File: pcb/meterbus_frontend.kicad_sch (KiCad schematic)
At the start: 34 parts, among them Q3 AO3400A, U1 78L05G, U3 ISO6721RBDR, U5 74HC14D

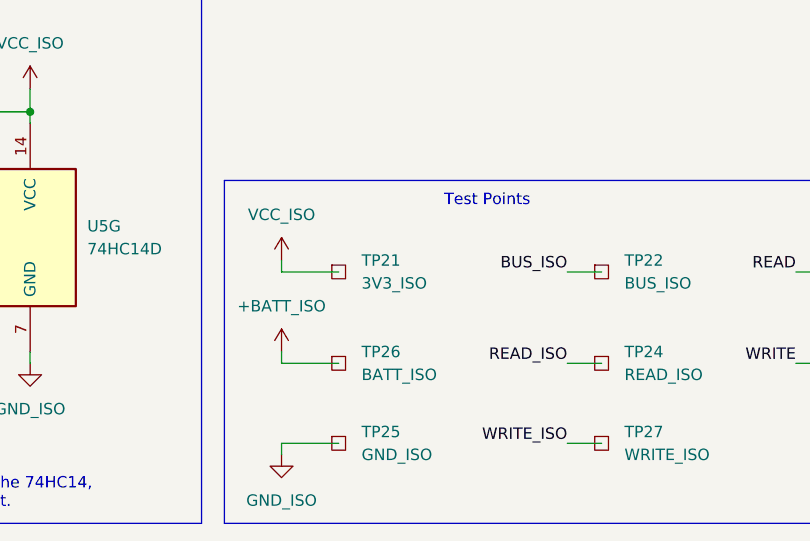
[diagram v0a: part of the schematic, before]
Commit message: sch: fix test point label
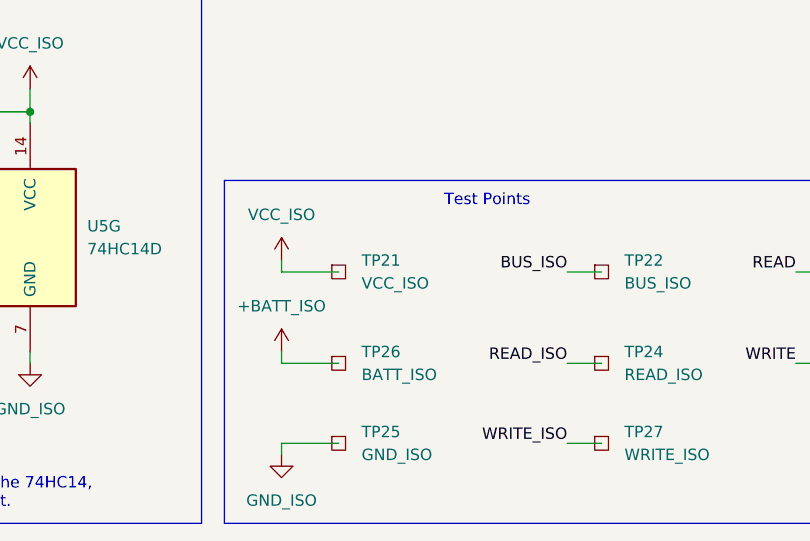
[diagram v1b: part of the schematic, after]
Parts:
- TP21: value 3V3_ISO -> VCC_ISO
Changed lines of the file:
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@@
 			)
 		)
-		(property "Value" "3V3_ISO"
+		(property "Value" "VCC_ISO"
 			(at 105.41 167.6399 0)
 			(show_name no)

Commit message: sch: rewire SPI to supply separate clock lines to flash and ethernet
The flash IC datasheet specifies that the SPI clock must not be toggled
while CS is high, which means we need to separate the ethernet and flash
clock lines.

I've GPIO3 on the ESP for the flash clock line, and plan to use the
internal peripheral MUX to switch it when talking with the IC.

I've also moved a bunch of test points and termination resistors in this
process.
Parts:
- TP21, TP22, TP24, TP25, TP26, TP27, TP28, TP29: now left out of the parts list

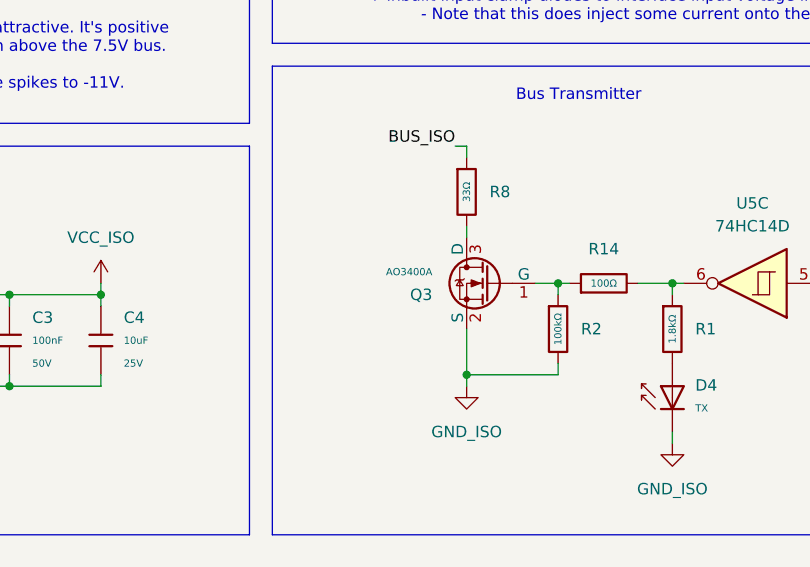
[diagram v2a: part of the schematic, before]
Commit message: sch: replace bus drive mosfet with 2N7002
The 2N7002 has higher voltage rating and costs less than the AO3400A.

It still has an appropriate 7 ohm RDSon @ 5V
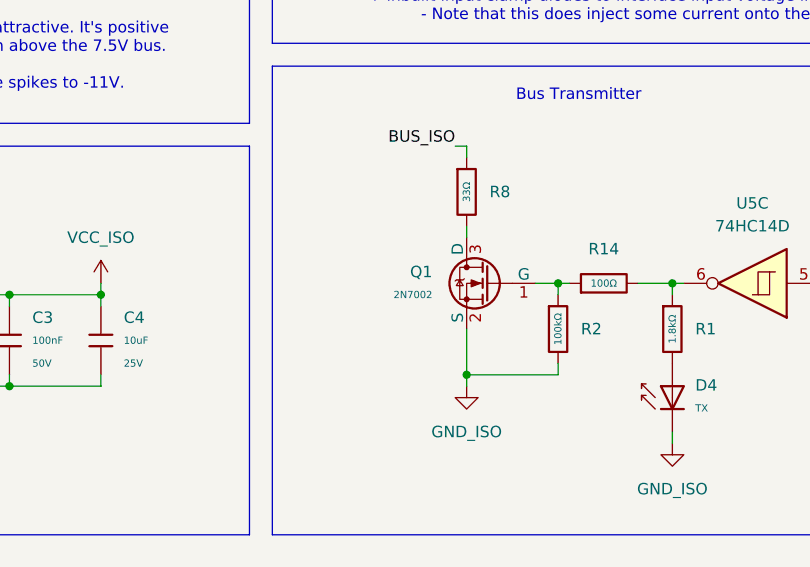
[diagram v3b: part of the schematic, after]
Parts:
- removed Q3: AO3400A, PCM_JLCPCB:Q_SOT-23, symbol PCM_JLCPCB-Transistors:NMOS,AO3400A
- added Q1: 2N7002, PCM_JLCPCB:Q_SOT-23, symbol PCM_JLCPCB-Transistors:NMOS,2N7002
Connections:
- net GND_ISO: now also Q1.2 (S)
- net at R14.1, R2.1: now also Q1.1 (G)
- net at R8.2: now also Q1.3 (D)

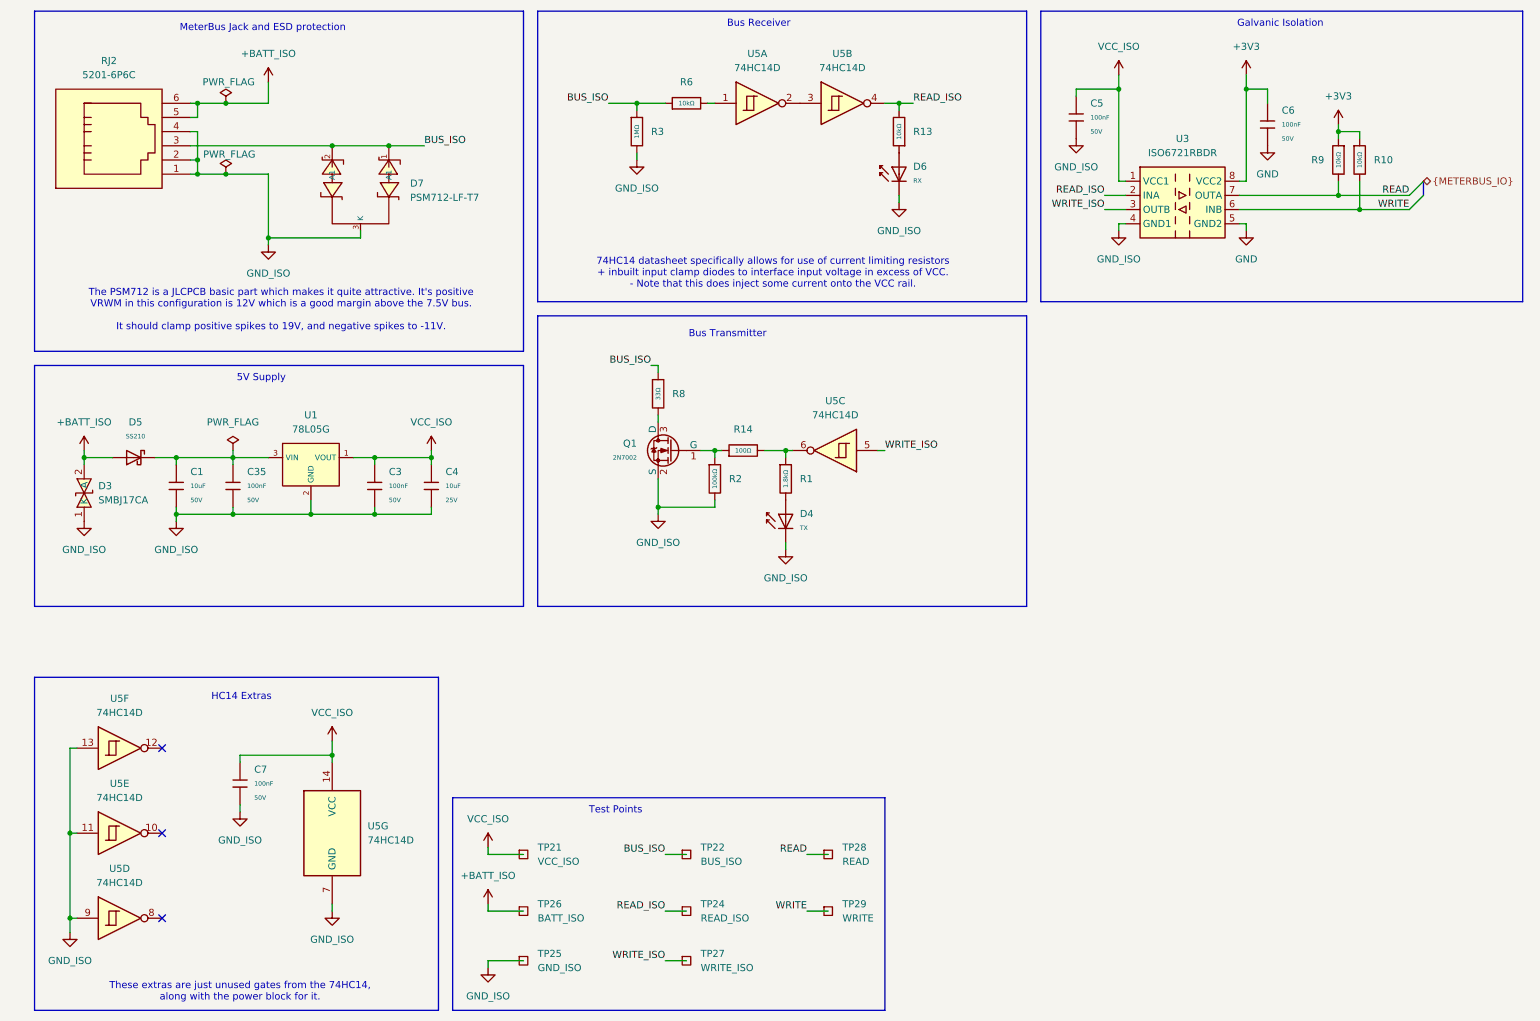
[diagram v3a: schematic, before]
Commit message: sch: rename meterbus power rail label
The old label BATT_ISO was a bit confusing, and I think MB_PWR_ISO is
more accurate
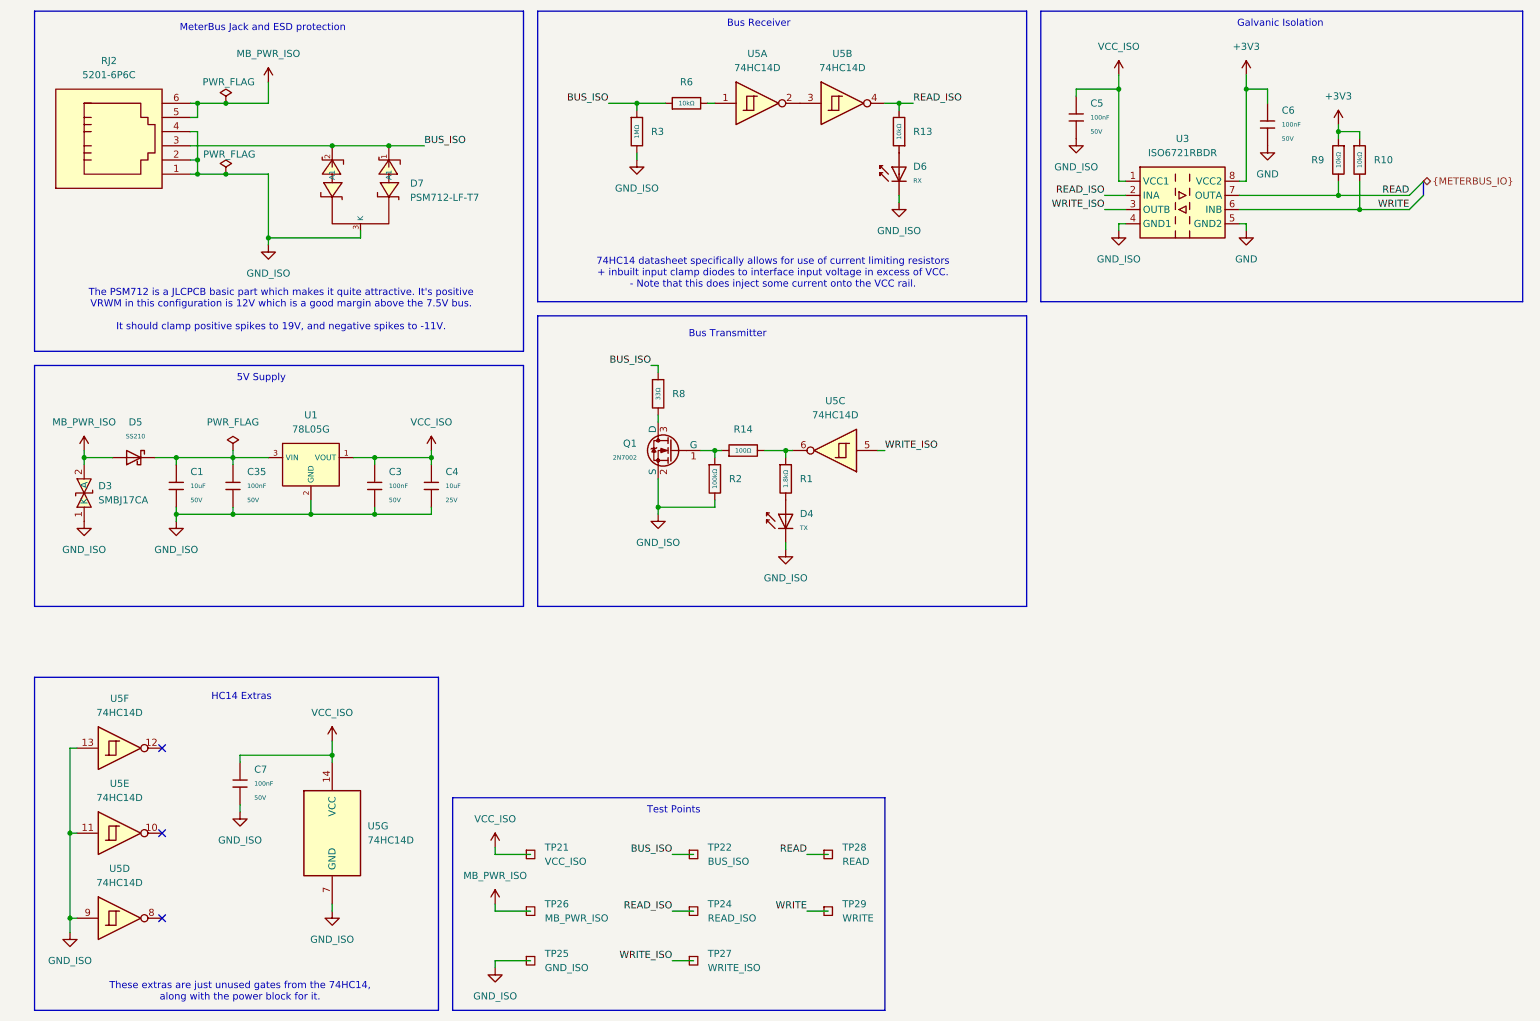
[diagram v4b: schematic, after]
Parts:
- TP26: value BATT_ISO -> MB_PWR_ISO
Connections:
- net +BATT_ISO renamed MB_PWR_ISO
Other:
- moved on the sheet: TP21, TP22, TP24, TP25, TP26, TP27

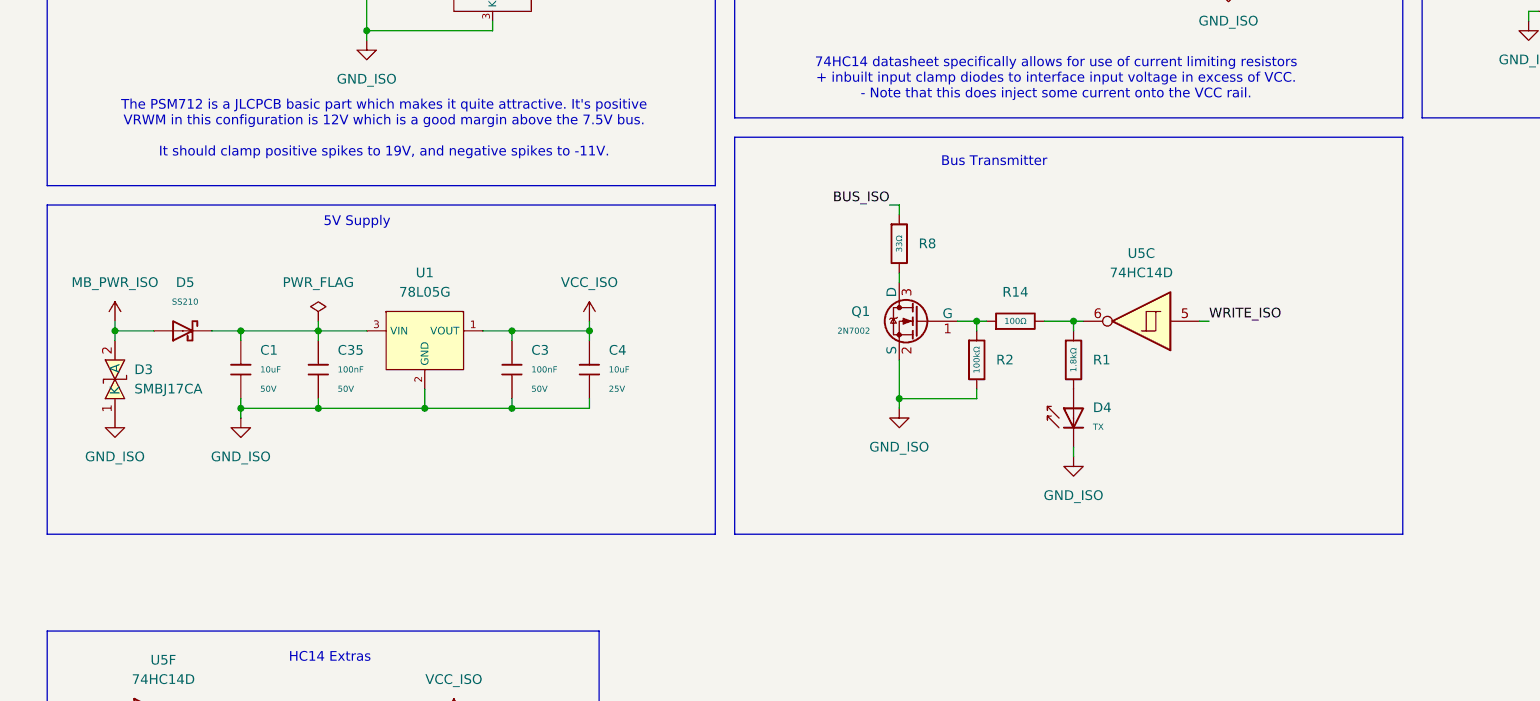
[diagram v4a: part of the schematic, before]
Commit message: sch: add note about meterbus power supply max voltage
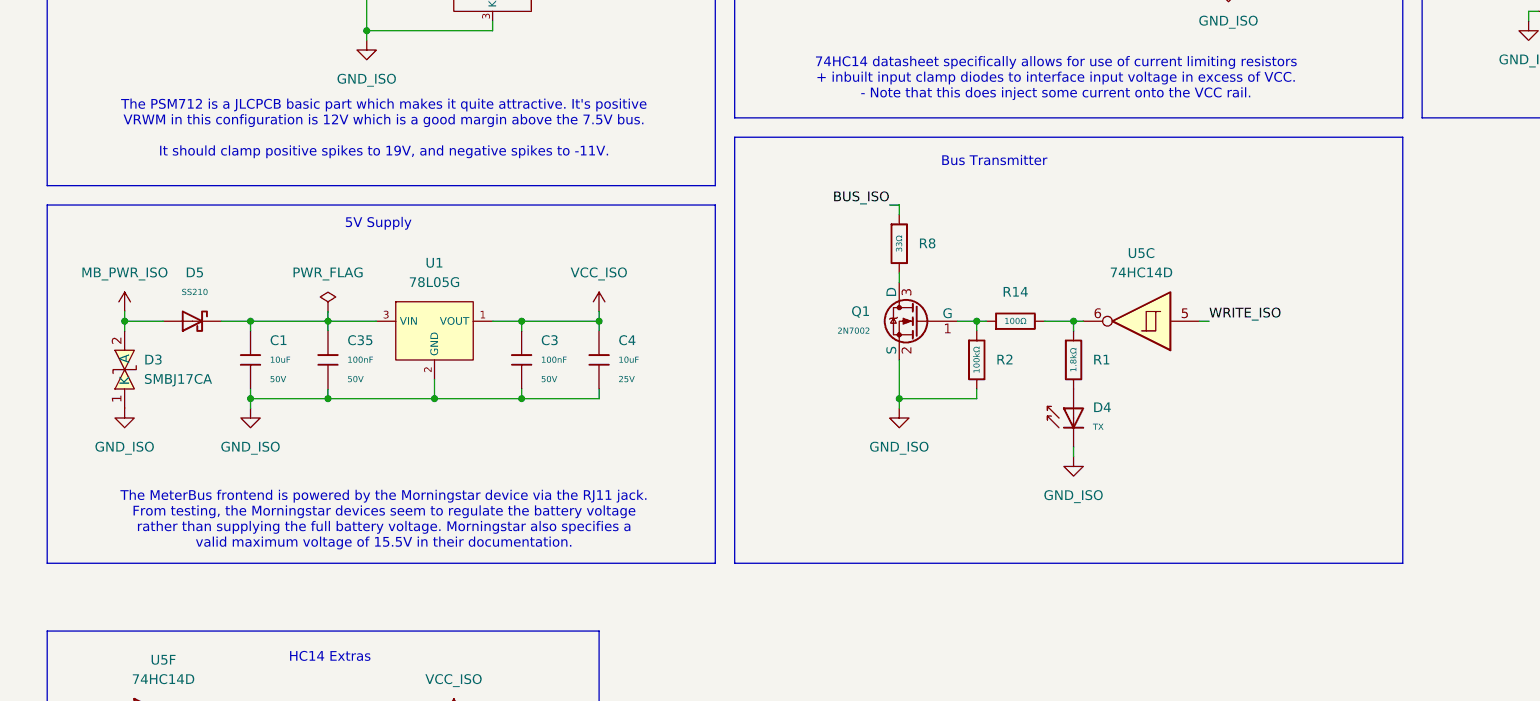
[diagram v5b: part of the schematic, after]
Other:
- note added: "The MeterBus frontend is powered by the Morningstar device via the RJ11 jack. From testing, the Morningstar devices seem to regulate the battery voltage rather than supplying the full battery voltage. Morningstar also specifies a valid maximum voltage of 15.5V in their documentation."
- moved on the sheet: C1, C3, C35, C4, D3, D5, U1
